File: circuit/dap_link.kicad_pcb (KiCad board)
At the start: 2 copper layers, 47.1 x 28.5 mm, 29 parts, among them J1 USB_A_CONN, J2 SWD_CONN_5P, J3 UART1_CONN_3P, J5 Conn_02x10_Odd_Even, U1 STM32F103CBTx, U2 AMS1117-3.3, U3 TXS0108EPW, Y1 8MHz

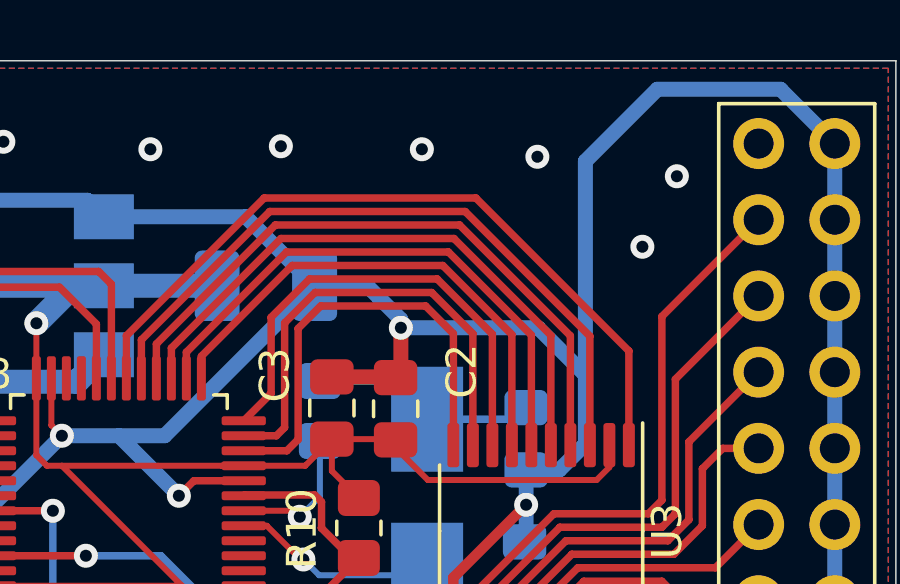
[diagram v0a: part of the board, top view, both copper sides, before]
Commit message: 板子加OE下拉 IO初始化修改
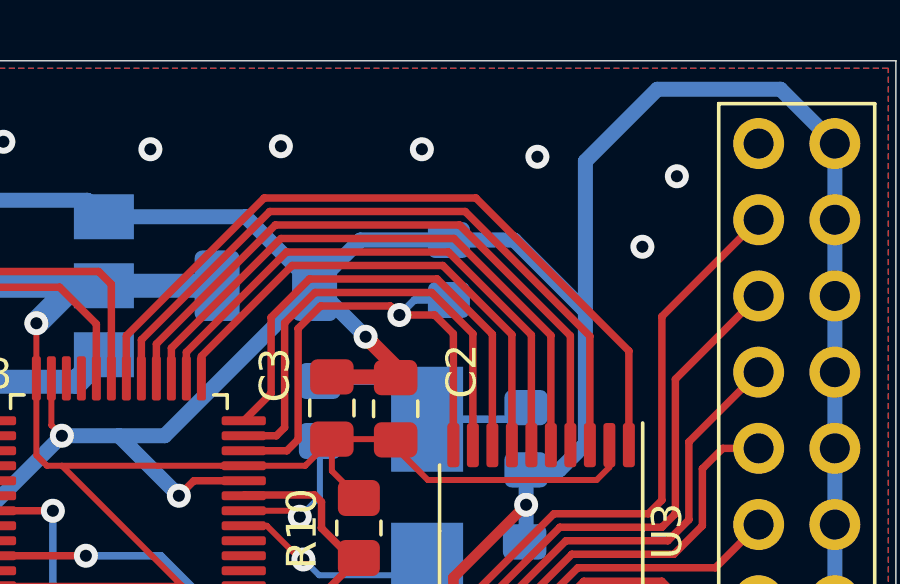
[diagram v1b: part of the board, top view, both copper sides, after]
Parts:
- added R11: 10K, Resistor_SMD:R_0805_2012Metric_Pad1.20x1.40mm_HandSolder, B.Cu at (123.7, 120.3)
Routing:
- net GND: track 157.9 -> 160.5 mm
- net /PA0: track 15.2 -> 17.1 mm, vias 0 -> 1

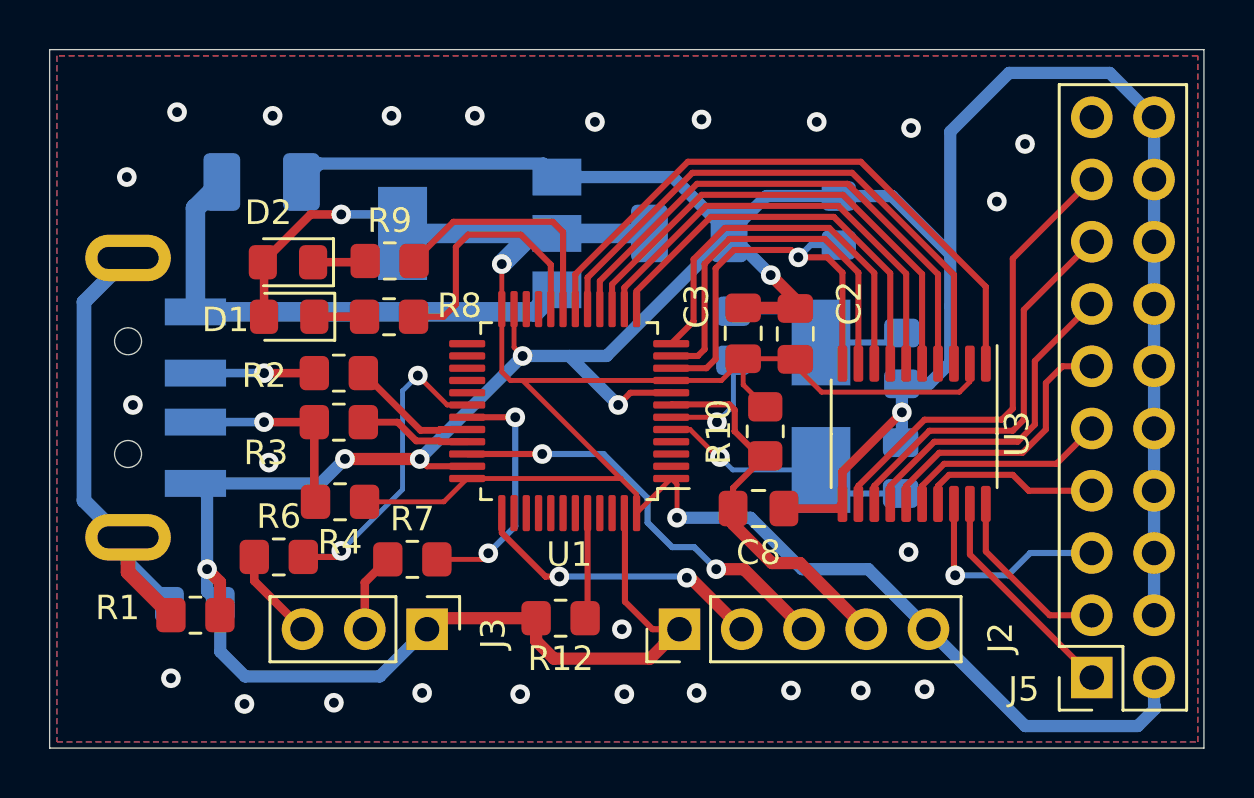
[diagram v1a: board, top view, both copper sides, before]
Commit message: 增加电源指示灯
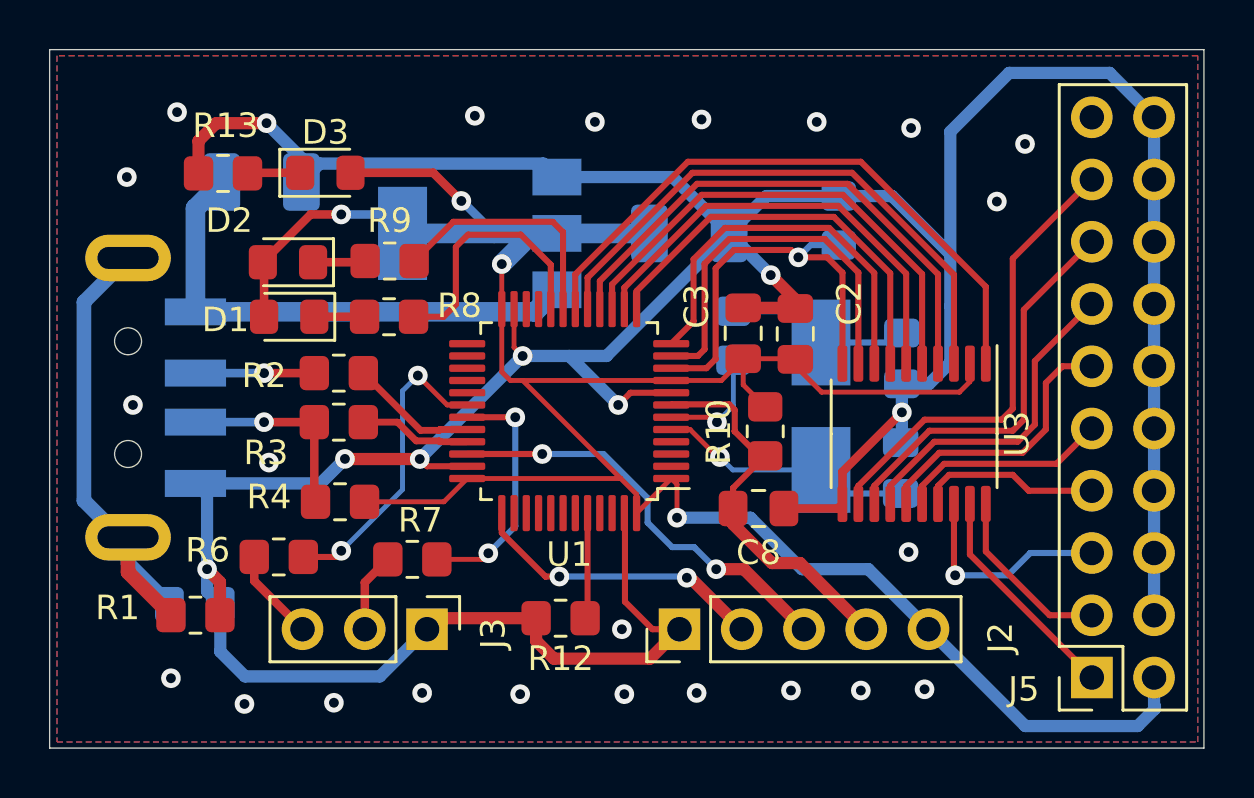
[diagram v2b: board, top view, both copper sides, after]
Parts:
- added D3: LEDB, Diode_SMD:D_0805_2012Metric_Pad1.15x1.40mm_HandSolder, F.Cu at (102.8, 118.3)
- added R13: 1K, Resistor_SMD:R_0805_2012Metric_Pad1.20x1.40mm_HandSolder, F.Cu at (98.6, 118.3)
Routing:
- net GND: track 160.5 -> 167.9 mm, vias 32 -> 31
- net +3V3: track 96.6 -> 103.5 mm, vias 3 -> 4
- net Net-(D3-K): track 0.00 -> 2.16 mm
